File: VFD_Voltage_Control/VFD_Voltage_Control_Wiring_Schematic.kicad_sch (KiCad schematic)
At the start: 11 parts

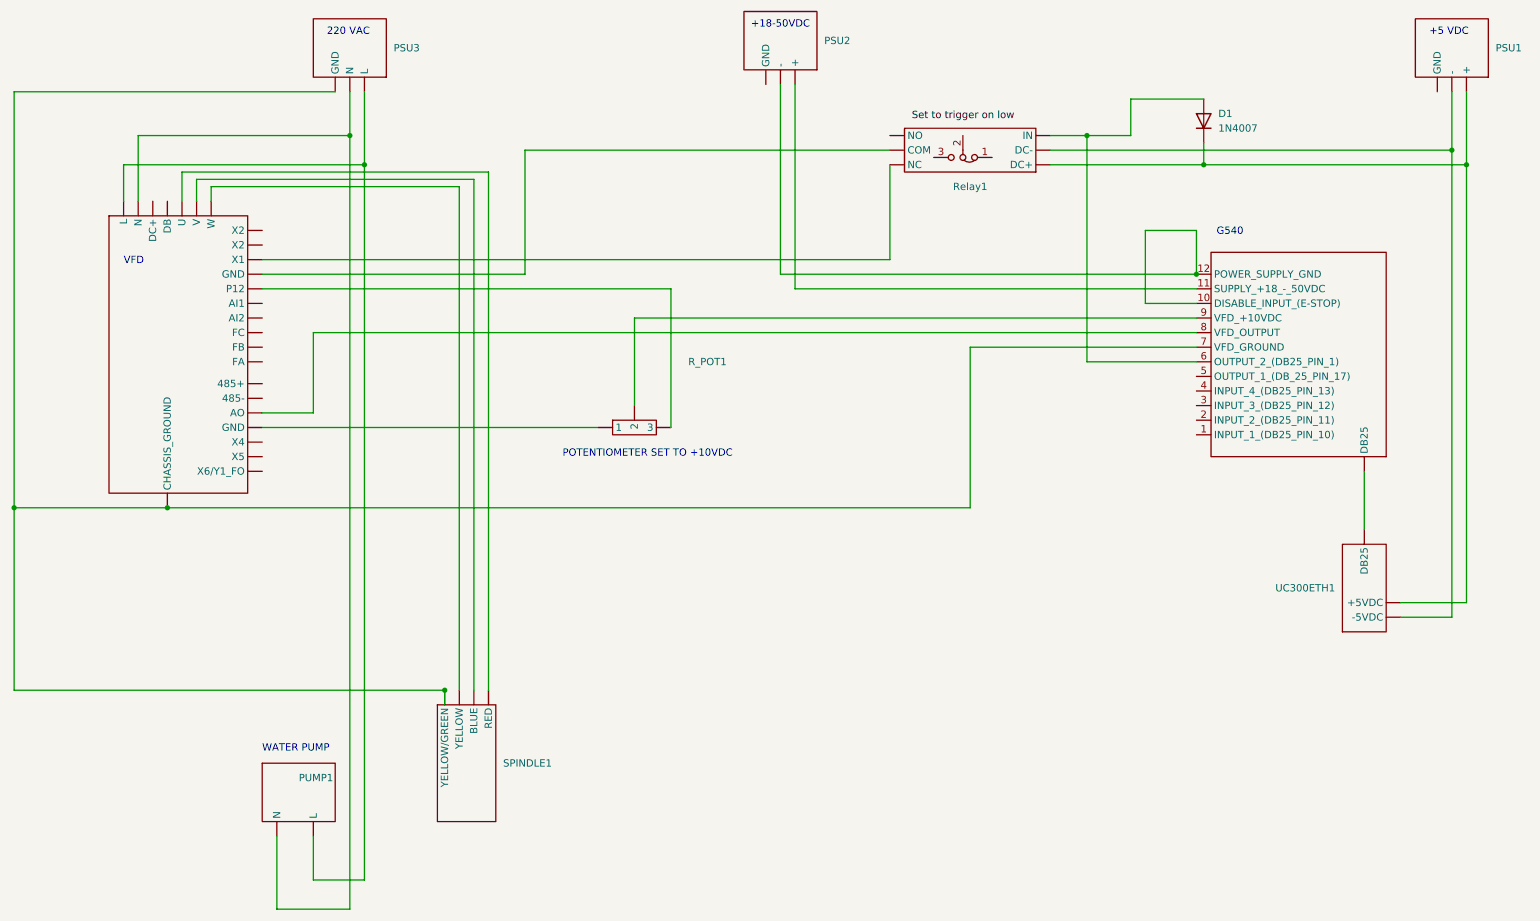
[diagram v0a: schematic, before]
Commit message: Got voltage control working using two relays.
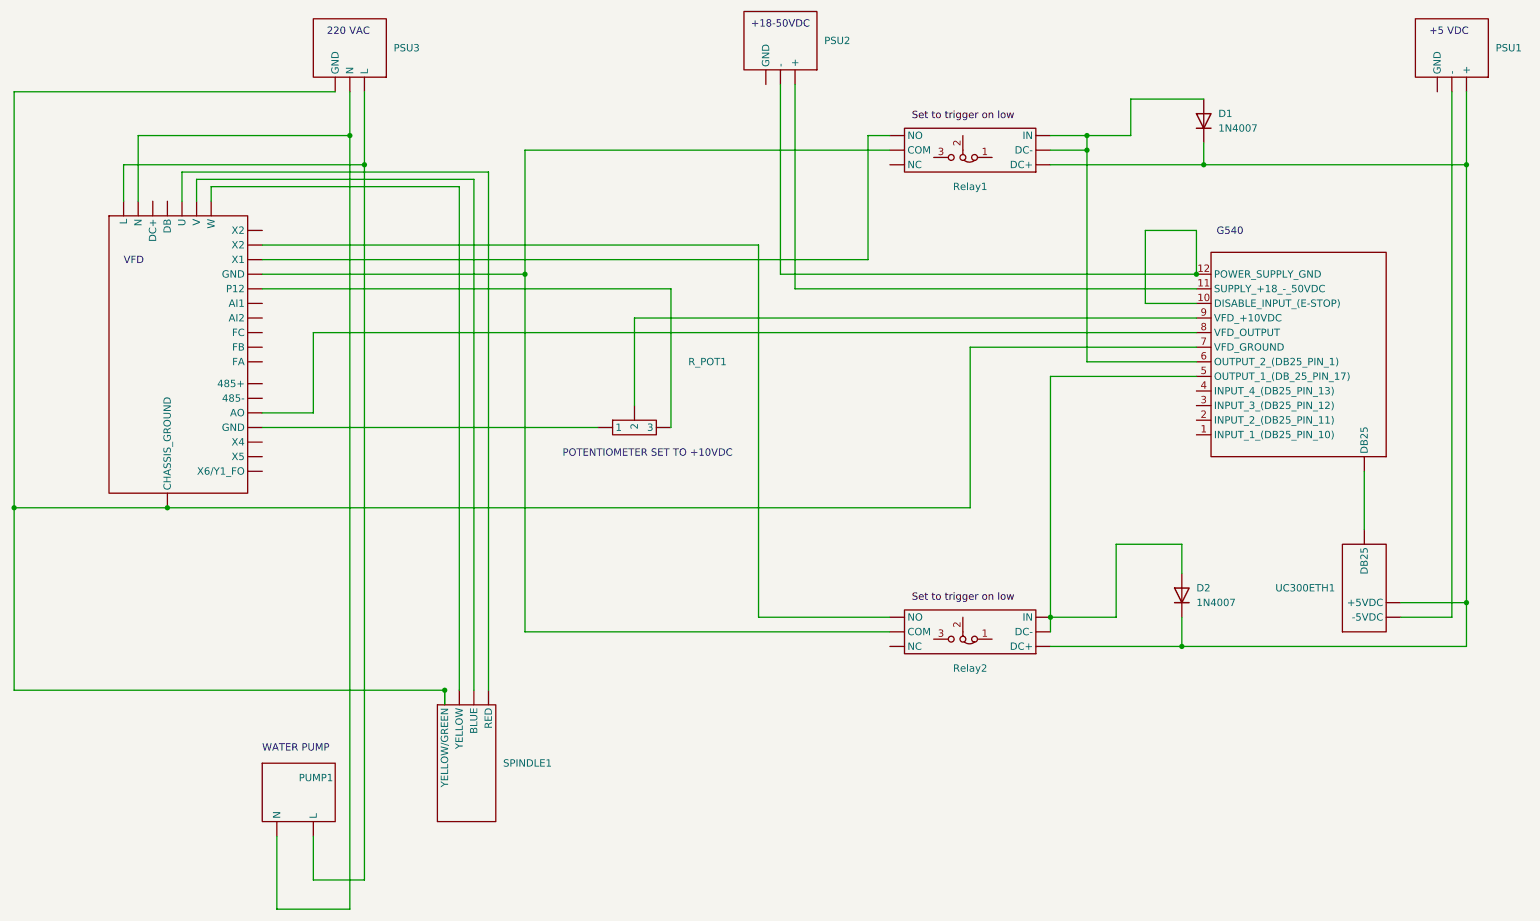
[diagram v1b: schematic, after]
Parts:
- added D2: 1N4007, Diode_THT:D_DO-41_SOD81_P10.16mm_Horizontal, symbol Diode:1N4007
- added Relay2: (no value), symbol Custom_Library:Relay
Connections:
- net at Relay1. (NO): now also VFD1. (X6/Y1_FO), Relay2. (NO)
- net at VFD1. (X6/Y1_FO): now also SPINDLE1. (RED); no longer Relay1. (NO)
- net at G1.5 (OUTPUT_1_(DB_25_PIN_17)): now also D2.2 (A), Relay2. (NO)
- new net: D1.1 (K), D2.1 (K), PSU1. (+), Relay1. (NO), Relay2. (NO), UC300ETH1. (DB25)
- new net: Relay1. (NO), VFD1. (X6/Y1_FO)
- new net: R_POT1. (3), VFD1. (X6/Y1_FO)
- new net: G1.7 (VFD_GROUND), PSU3. (L), SPINDLE1. (RED), VFD1. (X6/Y1_FO)
- new net: PSU3. (L), PUMP1. (L), VFD1. (X6/Y1_FO)
- new net: PSU1. (+), UC300ETH1. (DB25)
- new net: Relay2. (NO), VFD1. (X6/Y1_FO)
- new net: SPINDLE1. (RED), VFD1. (X6/Y1_FO) (x2)
- now unconnected: PSU1. (+), PSU1. (+)
